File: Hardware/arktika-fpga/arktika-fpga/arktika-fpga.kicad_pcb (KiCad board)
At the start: 4 copper layers, 131.8 x 81.3 mm, 130 parts

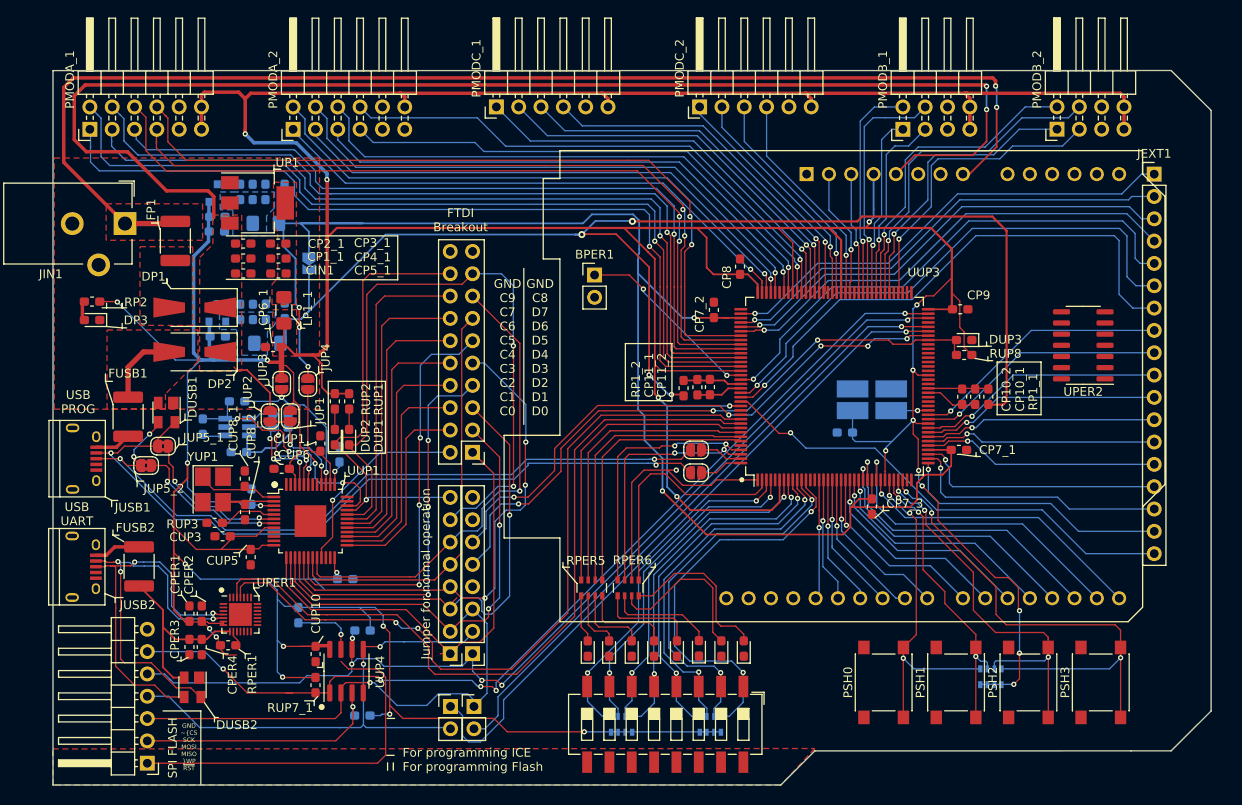
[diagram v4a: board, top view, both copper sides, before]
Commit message: Finished routing, did gnd planes, added more silkscreen and some manual via stitching. Pre-final layout.
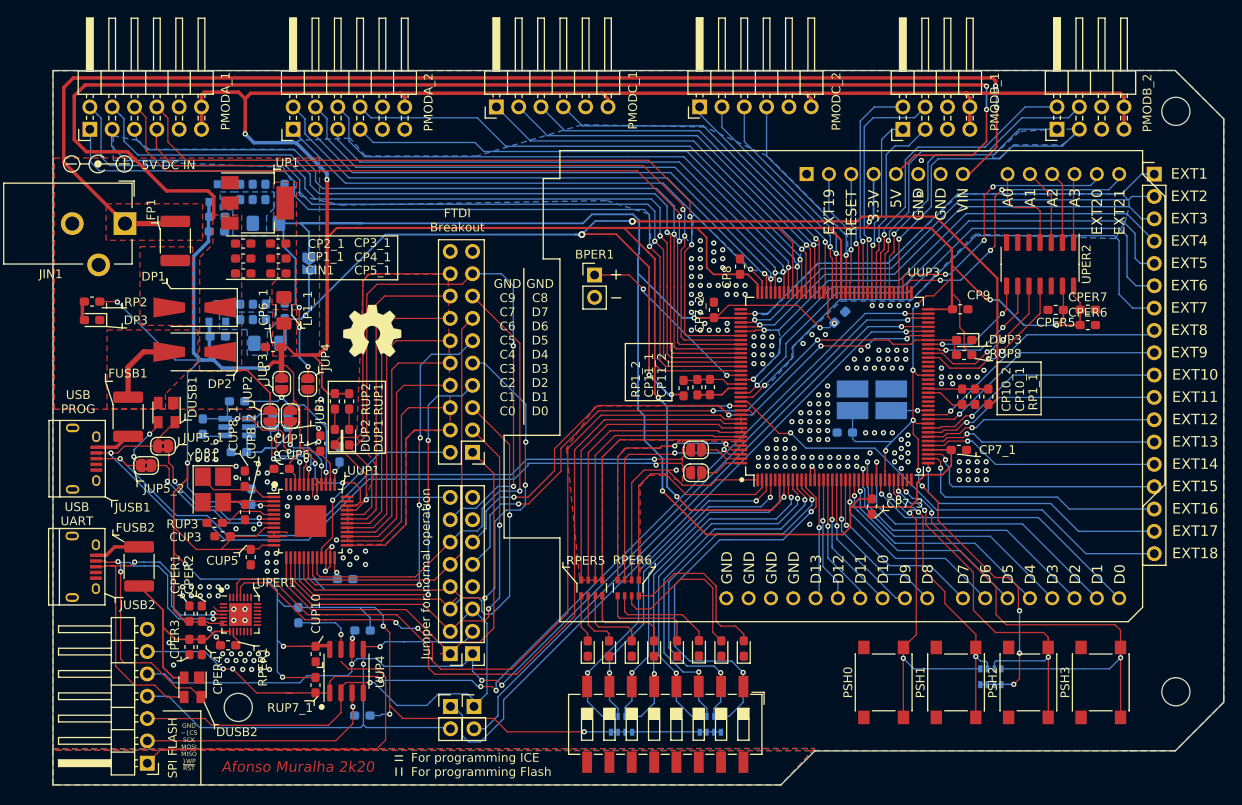
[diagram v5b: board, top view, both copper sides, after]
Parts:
- added CP7_4: 10n, Capacitor_SMD:C_0603_1608Metric_Pad1.05x0.95mm_HandSolder, B.Cu at (173.8, 85.7)
- added CPER5: 1u, Capacitor_SMD:C_0603_1608Metric_Pad1.05x0.95mm_HandSolder, F.Cu at (198.4, 84.8)
- added CPER6: 1u, Capacitor_SMD:C_0603_1608Metric_Pad1.05x0.95mm_HandSolder, F.Cu at (202.1, 86.5)
- added CPER7: 10u, Capacitor_SMD:C_0603_1608Metric_Pad1.05x0.95mm_HandSolder, F.Cu at (202.1, 84.8)
- added REF**: MountingHole_3.2mm_M3, MountingHole:MountingHole_3.2mm_M3, F.Cu at (105.4, 130.0)
- added REF**: MountingHole_3.2mm_M3, MountingHole:MountingHole_3.2mm_M3, F.Cu at (212.1, 128.3)
- added REF**: MountingHole_3.2mm_M3, MountingHole:MountingHole_3.2mm_M3, F.Cu at (212.1, 62.2)
- added REF**: OSHW-Symbol_6.7x6mm_SilkScreen, Symbol:OSHW-Symbol_6.7x6mm_SilkScreen, F.Cu at (120.6, 87.2)
- added REF**: Symbol_Barrel_Polarity, Symbol:Symbol_Barrel_Polarity, F.Cu at (89.5, 68.1)
- moved UPER2 10.4 mm to (196.6, 79.6), turned to 270 degrees
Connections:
- A1 pad 13: /FPGA_IO/ARDUINO_A4 -> /FPGA_IO/ARDUINO_EXTRA_4
- A1 pad 14: /FPGA_IO/ARDUINO_A5 -> /FPGA_IO/ARDUINO_EXTRA_3
- A1 pad 30: /FPGA_IO/ARDUINO_EXTRA_2 -> GND
- A1 pad 31: /FPGA_IO/ARDUINO_A4 -> GND
- A1 pad 32: /FPGA_IO/ARDUINO_A5 -> GND
- UPER2 pad 1: ADC_CH0 -> ADC_CH3
- UPER2 pad 2: ADC_CH1 -> ADC_CH2
- UPER2 pad 3: ADC_CH2 -> ADC_CH1
- UPER2 pad 4: ADC_CH3 -> ADC_CH0
- UUP3 pad 52: ADC_CH0 -> Net-(UUP3-Pad52)
- UUP3 pad 55: ADC_CH1 -> Net-(UUP3-Pad55)
- UUP3 pad 56: ADC_CH2 -> Net-(UUP3-Pad56)
- UUP3 pad 60: ADC_CH3 -> Net-(UUP3-Pad60)
- UUP3 pad 61: ADC_CS -> ADC_CLK
- UUP3 pad 62: ADC_MOSI -> ADC_MISO
- UUP3 pad 63: ADC_MISO -> ADC_MOSI
- UUP3 pad 64: ADC_CLK -> ADC_CS
- UUP3 pad 74: Net-(UUP3-Pad74) -> /FPGA_IO/ARDUINO_EXTRA_3
- UUP3 pad 75: Net-(UUP3-Pad75) -> /FPGA_IO/ARDUINO_EXTRA_4
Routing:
- net /FPGA_IO/ARDUINO_EXTRA_3: track 0.00 -> 33.9 mm, vias 0 -> 3
- net /FPGA_IO/ARDUINO_EXTRA_4: track 0.00 -> 32.0 mm, vias 0 -> 3
- net /VCC3V3: track 733.9 -> 761.3 mm, vias 30 -> 32
- net /Power/VCC_CORE: track 171.8 -> 193.7 mm, vias 5 -> 7
- net GND: track 0.00 -> 21.4 mm, vias 0 -> 236
- net ADC_CLK: track 0.00 -> 18.9 mm, vias 0 -> 2
- net ADC_MISO: track 0.00 -> 17.5 mm, vias 0 -> 2
- net ADC_MOSI: track 0.00 -> 15.0 mm, vias 0 -> 2
- net ADC_CS: track 0.00 -> 13.2 mm, vias 0 -> 2
- net ADC_CH0: track 0.00 -> 10.8 mm
- net ADC_CH1: track 0.00 -> 8.79 mm
- net ADC_CH2: track 0.00 -> 8.32 mm
- net ADC_CH3: track 0.00 -> 7.83 mm
- net /Power/VCC1.2_PLL: track 145.4 -> 139.9 mm
- net /Power/VCCPLL0: track 6.95 -> 9.84 mm
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- added copper zone on B.Cu, net (none)
- added copper zone on B.Cu, net GND
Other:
- board size 131.8 x 81.3 mm -> 133.2 x 81.3 mm
- board text added: "3.3V"
- board text added: "5V"
- board text added: "5V DC IN"
- board text added: "A0"
- board text added: "A1"
- board text added: "A2"
- board text added: "A3"
- board text added: "Afonso Muralha 2k20"
- board text added: "D0"
- board text added: "D1"
- board text added: "D10"
- board text added: "D11"
- board text added: "D12"
- board text added: "D13"
- board text added: "D2"
- board text added: "D3"
- board text added: "D4"
- board text added: "D5"
- board text added: "D6"
- board text added: "D7"
- board text added: "D8"
- board text added: "D9"
- board text added: "EXT1"
- board text added: "EXT10"
- board text added: "EXT11"
- board text added: "EXT12"
- board text added: "EXT13"
- board text added: "EXT14"
- board text added: "EXT15"
- board text added: "EXT16"
- board text added: "EXT17"
- board text added: "EXT18"
- board text added: "EXT19"
- board text added: "EXT2"
- board text added: "EXT20"
- board text added: "EXT21"
- board text added: "EXT3"
- board text added: "EXT4"
- board text added: "EXT5"
- board text added: "EXT6"
- board text added: "EXT7"
- board text added: "EXT8"
- board text added: "EXT9"
- board text added: "GND"
- board text added: "RESET"
- board text added: "VIN"

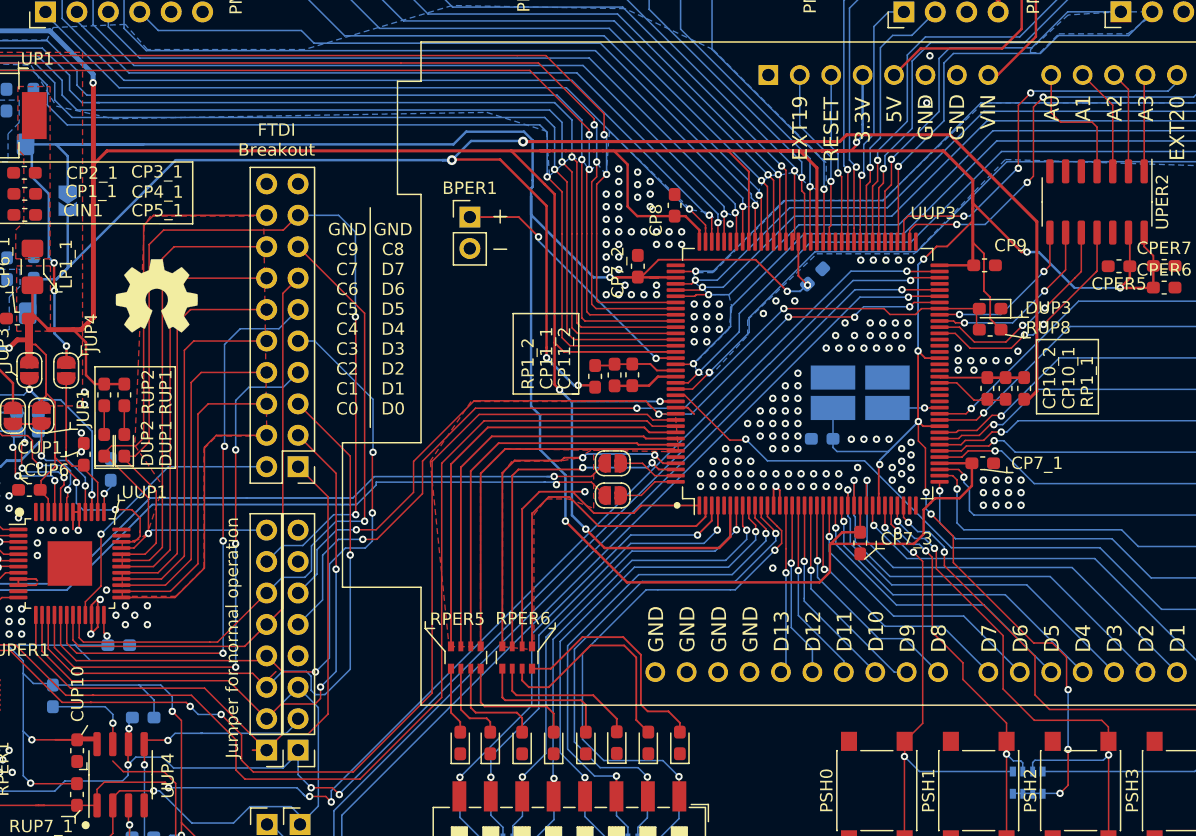
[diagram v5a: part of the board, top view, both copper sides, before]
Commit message: Minor layout fixes
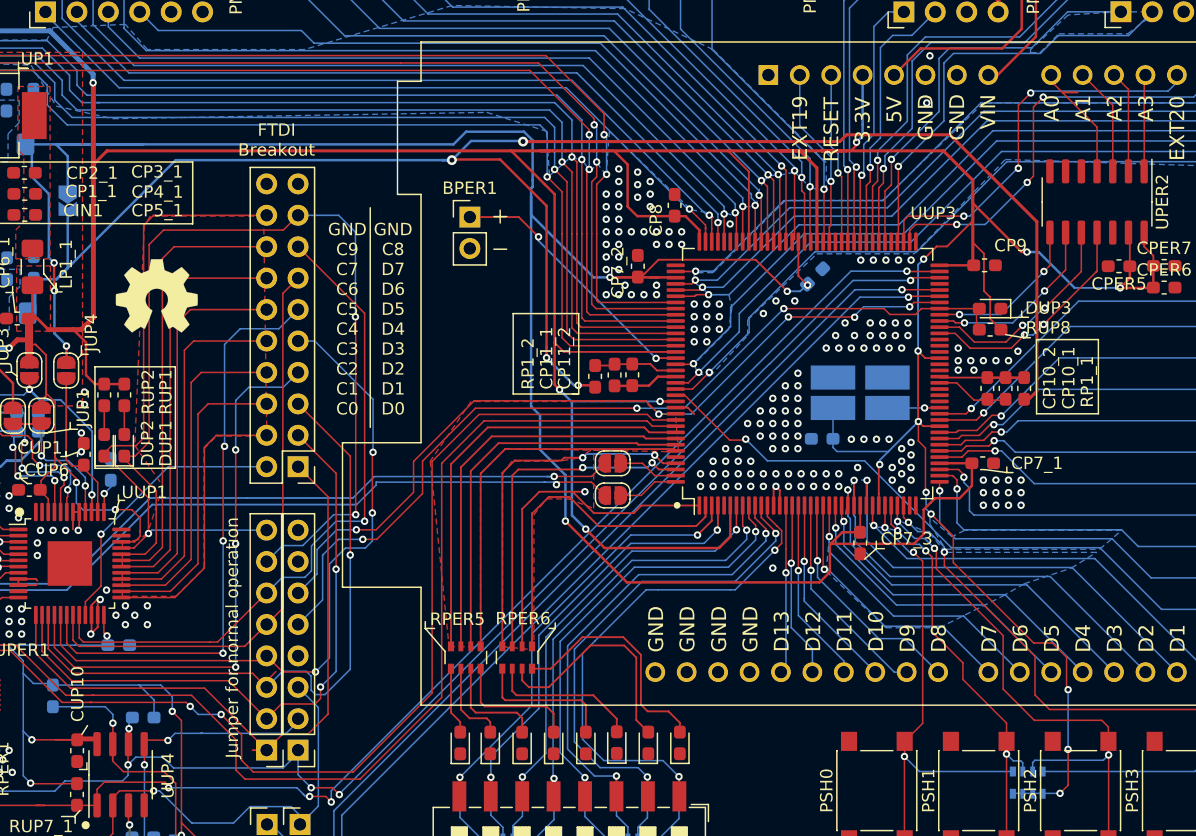
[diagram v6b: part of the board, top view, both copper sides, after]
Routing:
- net /VCC3V3: track 761.3 -> 759.7 mm
- net /USB AND PROG/FLASH_MISO: track 57.9 -> 56.2 mm
- net /USB AND PROG/flash_~RST: track 48.9 -> 50.3 mm
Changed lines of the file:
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@@
     (thickness 1.6002)
     (drawings 300)
-    (tracks 2589)
+    (tracks 2588)
     (zones 0)
     (modules 139)
@@
   (segment (start 122.6425 130.818) (end 121.7535 130.818) (width 0.125) (layer Back) (net 7))
   (segment (start 131.764 75.5) (end 132.399 75.5) (width 0.2) (layer Front) (net 7))
-  (segment (start 114.039 115.45) (end 115.2271 116.6381) (width 0.125) (layer Back) (net 7))
   (segment (start 176.375 75.5) (end 176 75.5) (width 0.25) (layer Front) (net 7))
   (segment (start 176 75.5) (end 174.4 75.5) (width 0.25) (layer Front) (net 7))
@@
   (segment (start 131.5 128.5) (end 128.175 128.5) (width 0.125) (layer Back) (net 60))
   (segment (start 132.225 129.94) (end 132.225 129.225) (width 0.125) (layer Back) (net 60))
-  (segment (start 132.0673 118.855) (end 130.8819 120.0404) (width 0.125) (layer Back) (net 60))
   (segment (start 132.0673 118.855) (end 133.7056 120.4933) (width 0.125) (layer Back) (net 60))
   (segment (start 133.7056 128.4594) (end 132.225 129.94) (width 0.125) (layer Back) (net 60))
@@
   (segment (start 95.0595 136.398) (end 96.6475 134.81) (width 0.125) (layer Front) (net 62))
   (segment (start 96.6475 134.81) (end 121.13 134.81) (width 0.125) (layer Front) (net 62))
+  (segment (start 117.09 123.45) (end 117.09 124.815) (width 0.15) (layer Front) (net 62))
   (via (at 181.5 88.1) (size 0.6) (drill 0.3) (layers Front Back) (net 64))
   (segment (start 183.9125 87.75) (end 181.85 87.75) (width 0.125) (layer Front) (net 64))
@@
   (segment (start 157.025 131.075) (end 157.925 131.075) (width 0.125) (layer Back) (net 167))
   (segment (start 155.25 129.3) (end 157.025 131.075) (width 0.125) (layer Back) (net 167))
+  (segment (start 192.935 69.875) (end 192.935 69.37) (width 0.125) (layer Front) (net 168))
+  (segment (start 193.84 70.78) (end 195.07 70.78) (width 0.15) (layer Front) (net 168))
+  (segment (start 193.84 70.78) (end 192.935 69.875) (width 0.125) (layer Front) (net 168))
+  (segment (start 196.64 77.155) (end 196.64 73.58) (width 0.125) (layer Front) (net 168))
+  (segment (start 196.64 73.58) (end 193.84 70.78) (width 0.125) (layer Front) (net 168))
   (segment (start 198.05 69.405) (end 198.015 69.37) (width 0.125) (layer Front) (net 170))
   (via (at 185.525 88.725) (size 0.6) (drill 0.3) (layers Front Back) (net 172))
@@
   (segment (start 181.025 81.125) (end 181.025 82.8125) (width 0.125) (layer Front) (net 217))
   (via (at 191 78.05) (size 0.6) (drill 0.3) (layers Front Back) (net 218))
-  (segment (start 192.935 72.425) (end 192.935 69.37) (width 0.125) (layer Front) (net 168))
-  (segment (start 193.69 73.18) (end 192.935 72.425) (width 0.125) (layer Front) (net 168))
-  (segment (start 196.64 73.58) (end 196.24 73.18) (width 0.125) (layer Front) (net 168))
-  (segment (start 196.64 77.155) (end 196.64 73.58) (width 0.125) (layer Front) (net 168))
-  (segment (start 196.24 73.18) (end 193.69 73.18) (width 0.125) (layer Front) (net 168))
   (segment (start 197.91 71.805) (end 197.3825 71.2775) (width 0.125) (layer Front) (net 169))
   (segment (start 195.475 69.37) (end 197.3825 71.2775) (width 0.125) (layer Front) (net 169))
@@
       )
     )
+    (polygon
+      (pts
+        (xy 177.038 102.108) (xy 176.53 102.87) (xy 176.276 105.41) (xy 175.006 106.68) (xy 174.752 109.474)
+        (xy 179.578 114.046) (xy 183.896 114.046) (xy 188.976 111.506) (xy 190.754 110.49) (xy 194.564 109.22)
+        (xy 196.596 107.95) (xy 184.404 107.95) (xy 183.134 106.426) (xy 181.356 105.664) (xy 180.594 105.41)
+        (xy 180.34 106.172) (xy 179.324 105.918) (xy 178.562 105.918) (xy 178.054 105.41) (xy 178.054 102.108)
+      )
+    )
+    (polygon
+      (pts
+        (xy 183.134 105.664) (xy 184.404 107.696) (xy 196.85 107.696) (xy 198.628 106.172) (xy 185.928 106.172)
+        (xy 184.912 106.68) (xy 183.134 105.156)
+      )
+    )

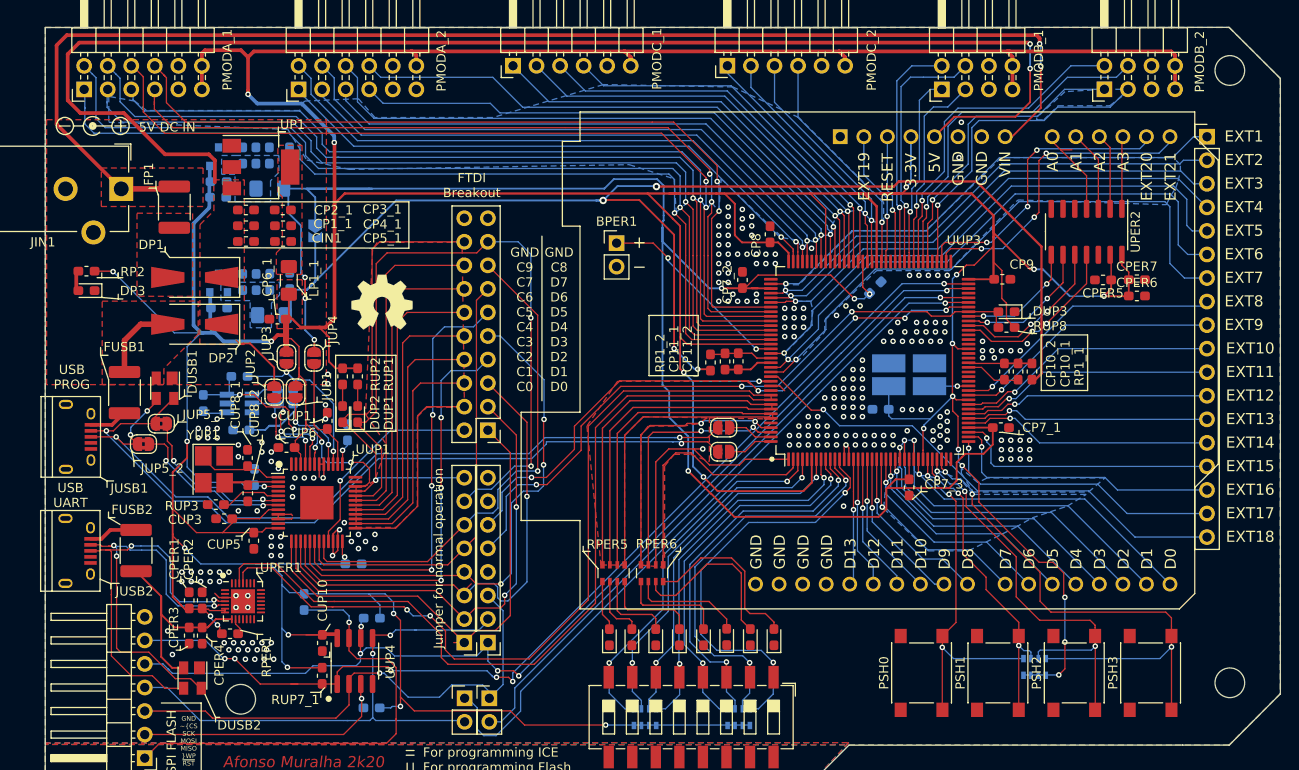
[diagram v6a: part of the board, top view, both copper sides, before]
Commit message: Fixed minor drc errors. removed usb jumpers and added needed resistors
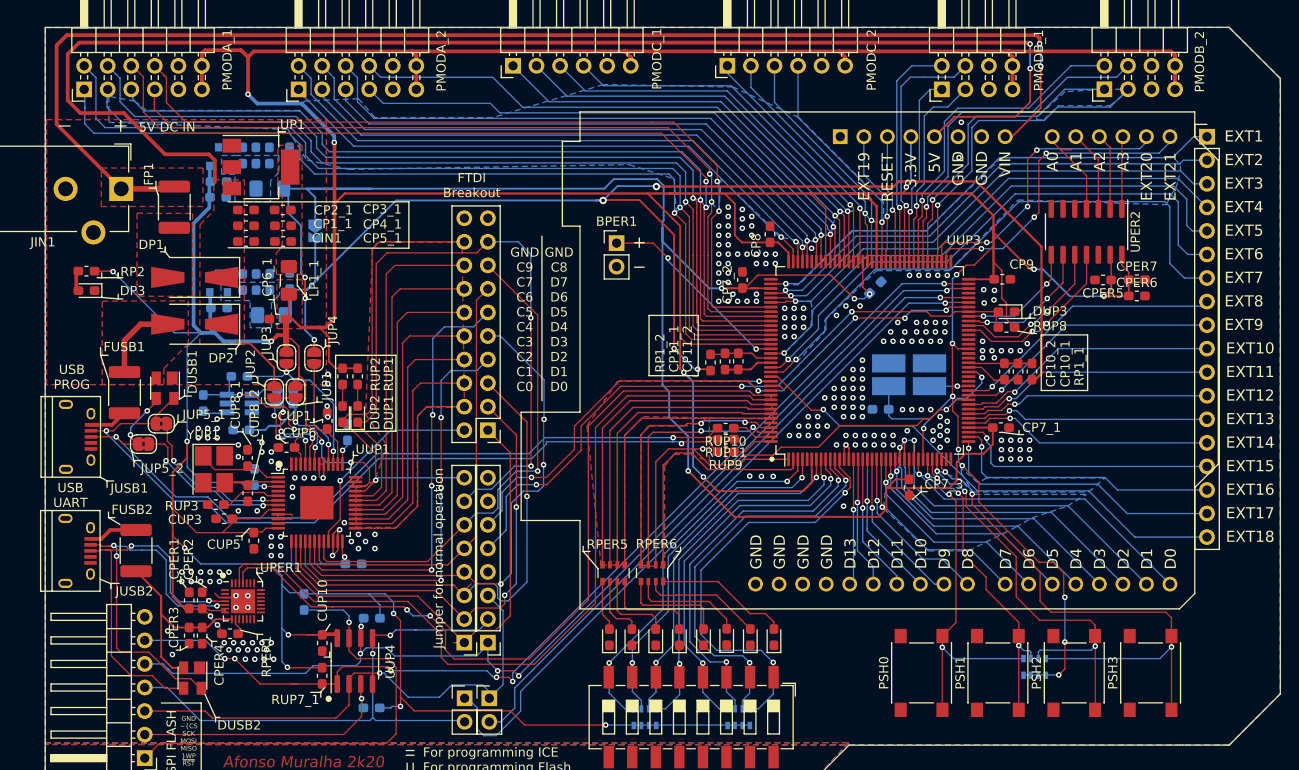
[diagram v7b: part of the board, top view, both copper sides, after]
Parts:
- removed JPUP6_2, JUP6_1: SolderJumper_2_Open, Jumper:SolderJumper-2_P1.3mm_Open_RoundedPad1.0x1.5mm
- removed REF** (x3): MountingHole_3.2mm_M3, MountingHole:MountingHole_3.2mm_M3
- removed REF**: OSHW-Symbol_6.7x6mm_SilkScreen, Symbol:OSHW-Symbol_6.7x6mm_SilkScreen
- removed REF**: Symbol_Barrel_Polarity, Symbol:Symbol_Barrel_Polarity
- added RUP10: 68, Resistor_SMD:R_0603_1608Metric_Pad1.05x0.95mm_HandSolder, F.Cu at (157.7, 100.8)
- added RUP11: 1.5k, Resistor_SMD:R_0603_1608Metric_Pad1.05x0.95mm_HandSolder, F.Cu at (157.7, 102.0)
- added RUP9: 68, Resistor_SMD:R_0603_1608Metric_Pad1.05x0.95mm_HandSolder, F.Cu at (157.7, 103.3)
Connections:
- UUP3 pad 52: Net-(UUP3-Pad52) -> /FPGA_IO/D+'
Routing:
- net /FPGA_IO/D+': track 0.00 -> 36.3 mm, vias 0 -> 2
- net Net-(D1-Pad2): track 18.6 -> 12.9 mm
- net /FPGA_PERIPHS/D+: track 41.3 -> 45.9 mm
- net Net-(D0-Pad2): track 19.0 -> 14.5 mm
- net /VCC3V3: track 759.7 -> 762.2 mm
- net /D+: track 84.4 -> 85.4 mm
- net /FPGA_PERIPHS/D-: track 41.7 -> 42.4 mm
- net GND: vias 236 -> 237
- net (no net): vias 3 -> 1
